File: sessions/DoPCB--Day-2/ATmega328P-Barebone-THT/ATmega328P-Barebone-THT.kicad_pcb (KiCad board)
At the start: 2 copper layers, 60.5 x 60.5 mm, 12 parts, among them J1 ISP, J2 PWR, U1 ATmega328P-PU, Y1 Crystal

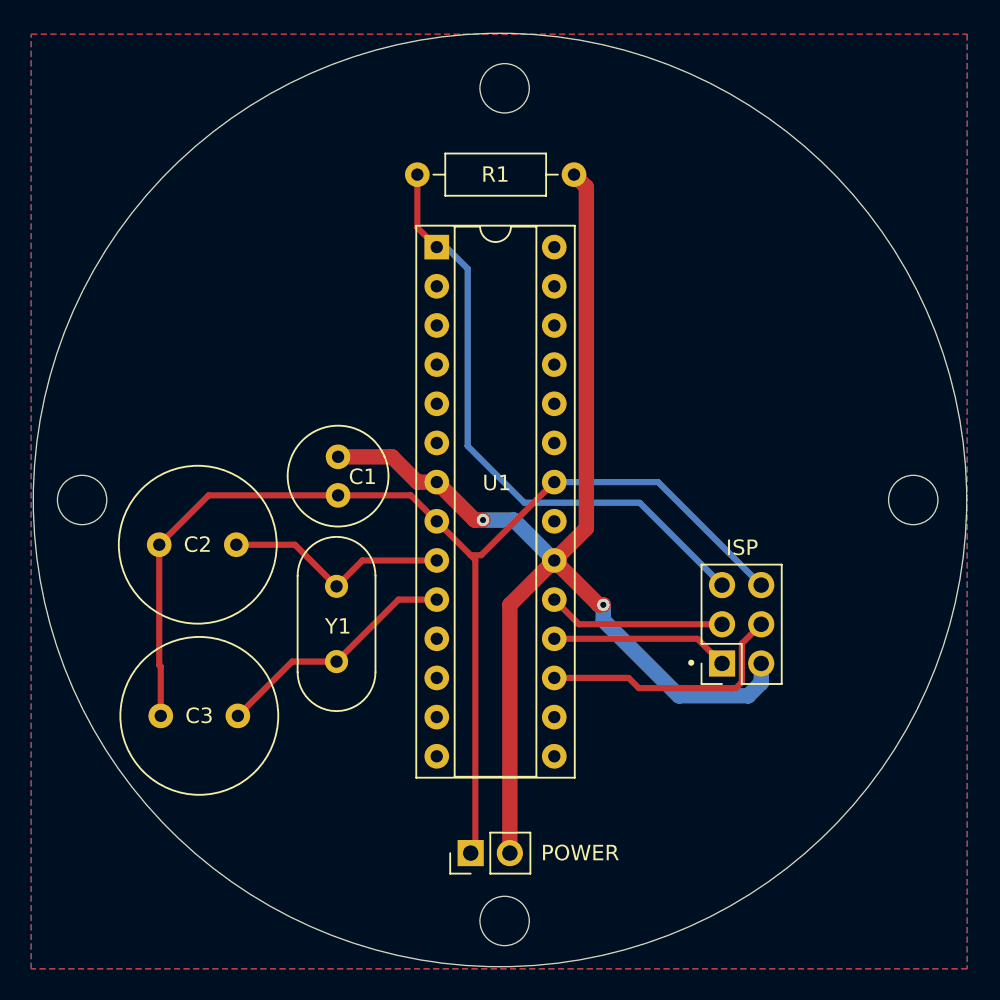
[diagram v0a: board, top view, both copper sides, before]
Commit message: updated day-2, added day-3
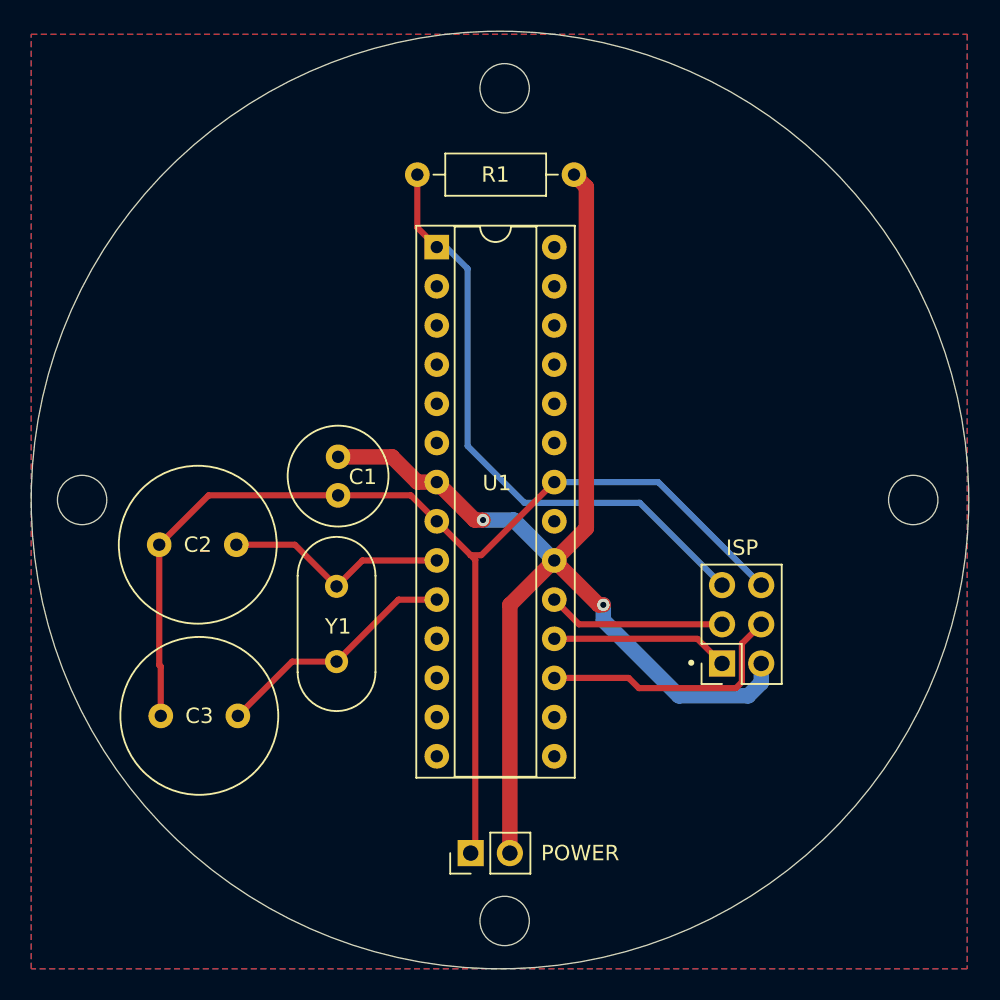
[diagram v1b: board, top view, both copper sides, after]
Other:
- board size 60.5 x 60.5 mm -> 60.8 x 60.8 mm
